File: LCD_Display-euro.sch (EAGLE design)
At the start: 4 parts, among them U1 NEWHAVEN_LCD

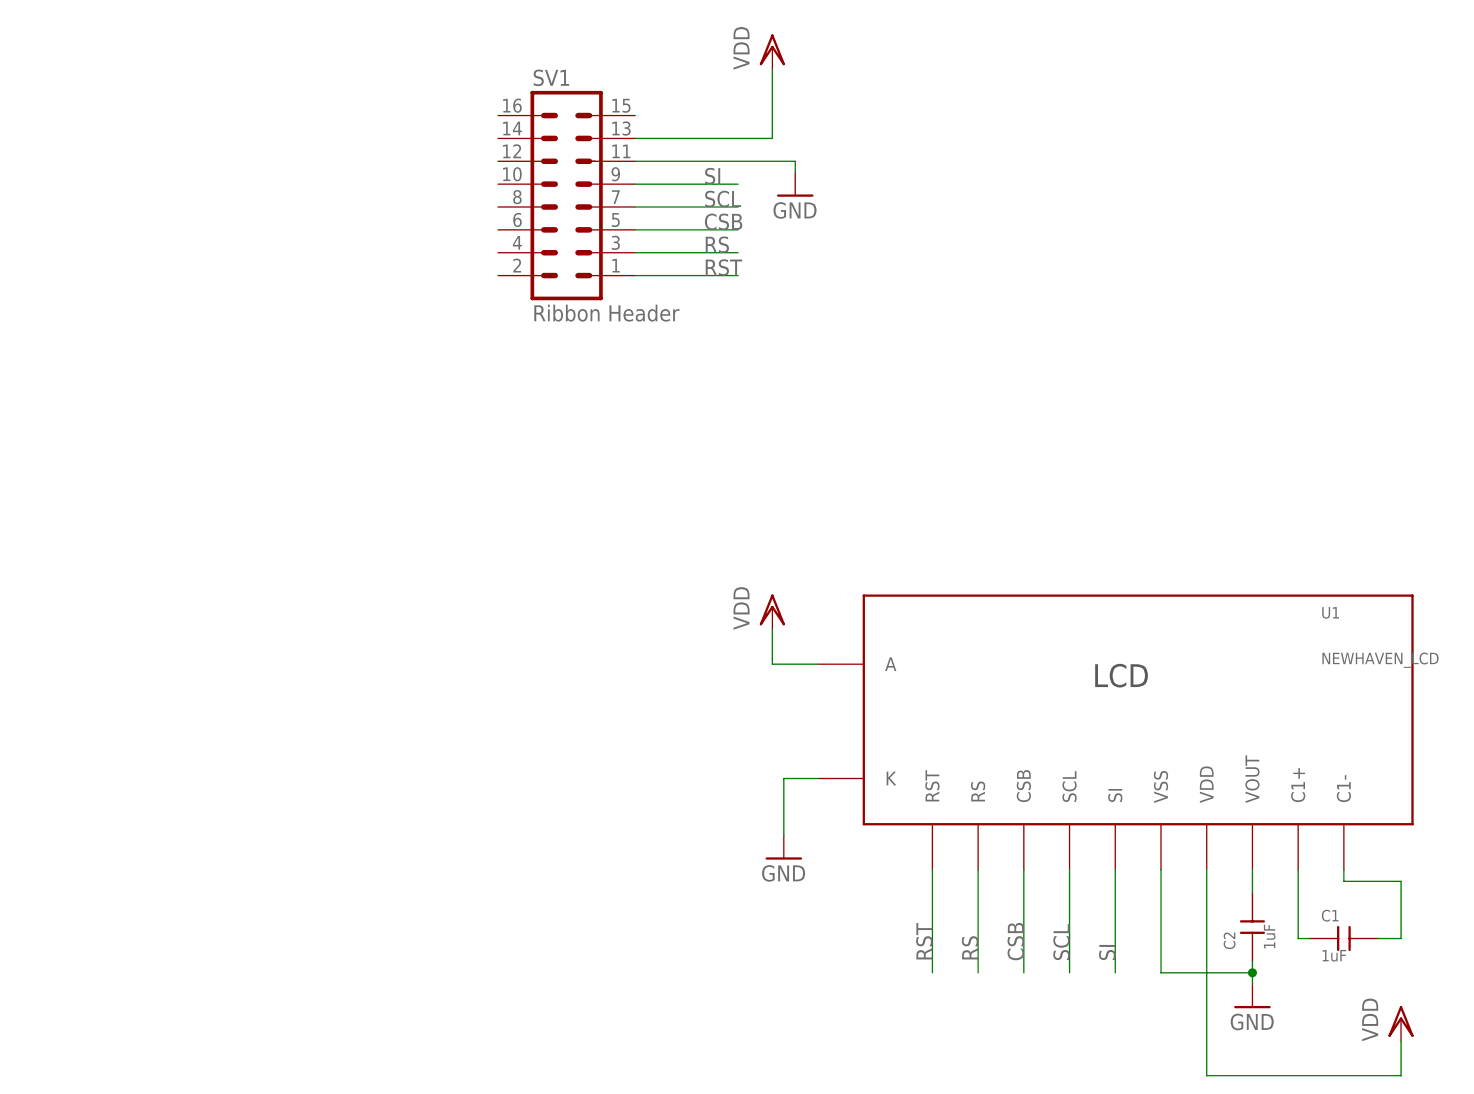
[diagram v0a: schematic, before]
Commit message: Fixed up Eurocard LCD module for production run
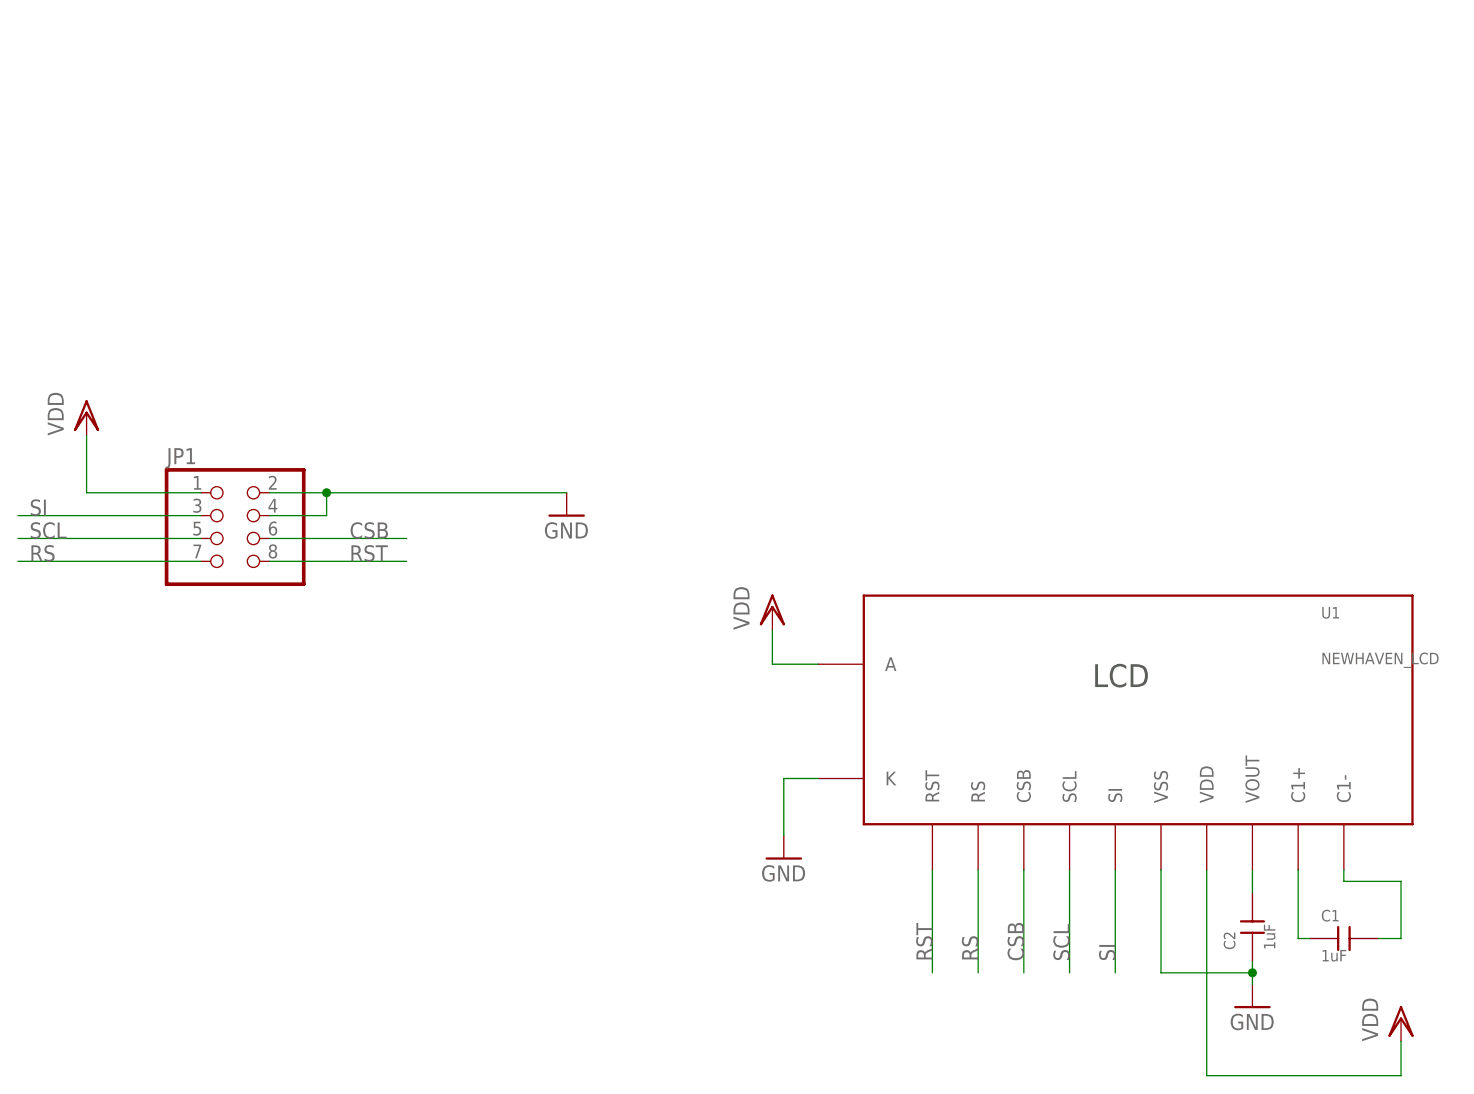
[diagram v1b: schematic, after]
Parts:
- removed SV1: Ribbon Header, mcu-accessories:ML16
- added JP1: (no value), mcu-accessories:PINHD-2X4SMT
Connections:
- net CSB: now also JP1.6; no longer SV1.5
- net GND: now also JP1.2, JP1.4; no longer SV1.11
- net RS: now also JP1.7; no longer SV1.3
- net RST: now also JP1.8; no longer SV1.1
- net SCL: now also JP1.5; no longer SV1.7
- net SI: now also JP1.3; no longer SV1.9
- net VDD: now also JP1.1; no longer SV1.13
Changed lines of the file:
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@@
 <?xml version="1.0" encoding="utf-8"?>
 <!DOCTYPE eagle SYSTEM "eagle.dtd">
-<eagle version="6.5.0">
+<eagle version="6.6.0">
 <drawing>
 <settings>
@@
 <setting verticaltext="up"/>
 </settings>
-<grid distance="0.05" unitdist="inch" unit="inch" style="lines" multiple="1" display="no" altdistance="0.01" altunitdist="inch" altunit="inch"/>
+<grid distance="0.1" unitdist="inch" unit="inch" style="lines" multiple="1" display="no" altdistance="0.01" altunitdist="inch" altunit="inch"/>
 <layers>
 <layer number="1" name="Top" color="4" fill="1" visible="no" active="no"/>
@@
 <parts>
 <part name="U1" library="mcu-accessories" deviceset="NEWHAVEN_LCD" device=""/>
-<part name="SV1" library="mcu-accessories" deviceset="ML16" device="" value="Ribbon Header">
-<attribute name="PARTNO" value="S9171-ND"/>
-</part>
 <part name="C1" library="rlc-jqi" deviceset="CAP" device="0805" value="1uF">
 <attribute name="PARTNO" value="1276-2396-1-ND"/>
@@
 <part name="VDD1" library="supply1" deviceset="VDD" device=""/>
 <part name="VDD2" library="supply1" deviceset="VDD" device=""/>
-<part name="VDD3" library="supply1" deviceset="VDD" device=""/>
-<part name="GND3" library="supply1" deviceset="GND" device=""/>
+<part name="JP1" library="mcu-accessories" deviceset="PINHD-2X4" device="SMT"/>
+<part name="VDD4" library="supply1" deviceset="VDD" device=""/>
+<part name="GND4" library="supply1" deviceset="GND" device=""/>
 </parts>
 <sheets>
@@
 <instances>
 <instance part="U1" gate="G$1" x="68.58" y="59.69"/>
-<instance part="SV1" gate="1" x="2.54" y="118.11">
-<attribute name="PARTNO" x="2.54" y="118.11" size="1.778" layer="96" display="off"/>
-</instance>
 <instance part="C1" gate="G$1" x="88.9" y="34.29">
 <attribute name="PARTNO" x="88.9" y="34.29" size="1.778" layer="96" display="off"/>
@@
 <instance part="VDD1" gate="G$1" x="25.4" y="71.12"/>
 <instance part="VDD2" gate="G$1" x="95.25" y="25.4"/>
-<instance part="VDD3" gate="G$1" x="25.4" y="133.35"/>
-<instance part="GND3" gate="1" x="27.94" y="116.84"/>
+<instance part="JP1" gate="A" x="-35.56" y="78.74"/>
+<instance part="VDD4" gate="G$1" x="-50.8" y="92.71"/>
+<instance part="GND4" gate="1" x="2.54" y="81.28"/>
 </instances>
 <busses>
@@
 </segment>
 <segment>
-<pinref part="SV1" gate="1" pin="11"/>
-<wire x1="10.16" y1="120.65" x2="27.94" y2="120.65" width="0.1524" layer="91"/>
-<pinref part="GND3" gate="1" pin="GND"/>
-<wire x1="27.94" y1="120.65" x2="27.94" y2="119.38" width="0.1524" layer="91"/>
+<pinref part="JP1" gate="A" pin="2"/>
+<pinref part="GND4" gate="1" pin="GND"/>
+<wire x1="-30.48" y1="83.82" x2="-24.13" y2="83.82" width="0.1524" layer="91"/>
+<pinref part="JP1" gate="A" pin="4"/>
+<wire x1="-24.13" y1="83.82" x2="2.54" y2="83.82" width="0.1524" layer="91"/>
+<wire x1="-30.48" y1="81.28" x2="-24.13" y2="81.28" width="0.1524" layer="91"/>
+<wire x1="-24.13" y1="81.28" x2="-24.13" y2="83.82" width="0.1524" layer="91"/>
+<junction x="-24.13" y="83.82"/>
 </segment>
 </net>
@@
 </segment>
 <segment>
-<pinref part="SV1" gate="1" pin="13"/>
-<wire x1="10.16" y1="123.19" x2="25.4" y2="123.19" width="0.1524" layer="91"/>
-<pinref part="VDD3" gate="G$1" pin="VDD"/>
-<wire x1="25.4" y1="123.19" x2="25.4" y2="130.81" width="0.1524" layer="91"/>
+<pinref part="VDD4" gate="G$1" pin="VDD"/>
+<wire x1="-50.8" y1="90.17" x2="-50.8" y2="83.82" width="0.1524" layer="91"/>
+<pinref part="JP1" gate="A" pin="1"/>
+<wire x1="-50.8" y1="83.82" x2="-38.1" y2="83.82" width="0.1524" layer="91"/>
 </segment>
 </net>
@@
 </segment>
 <segment>
-<pinref part="SV1" gate="1" pin="9"/>
-<wire x1="10.16" y1="118.11" x2="21.59" y2="118.11" width="0.1524" layer="91"/>
-<label x="17.78" y="118.11" size="1.778" layer="95"/>
+<pinref part="JP1" gate="A" pin="3"/>
+<wire x1="-38.1" y1="81.28" x2="-58.42" y2="81.28" width="0.1524" layer="91"/>
+<label x="-57.15" y="81.28" size="1.778" layer="95"/>
 </segment>
 </net>
@@
 </segment>
 <segment>
-<pinref part="SV1" gate="1" pin="7"/>
-<wire x1="10.16" y1="115.57" x2="21.59" y2="115.57" width="0.1524" layer="91"/>
-<label x="17.78" y="115.57" size="1.778" layer="95"/>
+<pinref part="JP1" gate="A" pin="5"/>
+<wire x1="-38.1" y1="78.74" x2="-58.42" y2="78.74" width="0.1524" layer="91"/>
+<label x="-57.15" y="78.74" size="1.778" layer="95"/>
 </segment>
 </net>
@@
 </segment>
 <segment>
-<pinref part="SV1" gate="1" pin="5"/>
-<wire x1="10.16" y1="113.03" x2="21.59" y2="113.03" width="0.1524" layer="91"/>
-<label x="17.78" y="113.03" size="1.778" layer="95"/>
+<pinref part="JP1" gate="A" pin="6"/>
+<wire x1="-30.48" y1="78.74" x2="-15.24" y2="78.74" width="0.1524" layer="91"/>
+<label x="-21.59" y="78.74" size="1.778" layer="95"/>
 </segment>
 </net>
@@
 </segment>
 <segment>
-<pinref part="SV1" gate="1" pin="3"/>
-<wire x1="10.16" y1="110.49" x2="21.59" y2="110.49" width="0.1524" layer="91"/>
-<label x="17.78" y="110.49" size="1.778" layer="95"/>
+<pinref part="JP1" gate="A" pin="7"/>
+<wire x1="-38.1" y1="76.2" x2="-58.42" y2="76.2" width="0.1524" layer="91"/>
+<label x="-57.15" y="76.2" size="1.778" layer="95"/>
 </segment>
 </net>
@@
 </segment>
 <segment>
-<pinref part="SV1" gate="1" pin="1"/>
-<wire x1="10.16" y1="107.95" x2="21.59" y2="107.95" width="0.1524" layer="91"/>
-<label x="17.78" y="107.95" size="1.778" layer="95"/>
-</segment>
-</net>
+<pinref part="JP1" gate="A" pin="8"/>
+<wire x1="-30.48" y1="76.2" x2="-15.24" y2="76.2" width="0.1524" layer="91"/>
+<label x="-21.59" y="76.2" size="1.778" layer="95"/>
+</segment>
+</net>
